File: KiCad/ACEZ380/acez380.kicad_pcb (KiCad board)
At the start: 2 copper layers, 160 x 160.8 mm, 143 parts, among them IC1 LM7805_TO220, J300 Conn_02x06_Odd_Even, J301 Conn_02x05_Odd_Even, J303 Conn_02x03_Odd_Even, J304 Conn_02x05_Odd_Even, J400 48409-0003, J402 Conn_02x06_Odd_Even, J501 Conn_02x05_Odd_Even, J502 Conn_02x03_Odd_Even, Q1 2N3904, Q100 2N3904, Q3 BC183, X1 CRYSTALHC49U-V 6.556MHz, X2 20MHz

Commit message: Remove SMD.
Standardise Z180 and add Z380.


Signed-off-by: John Bradley <flypie@rocketmail.com>
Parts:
- added J503: Conn_02x05_Odd_Even, Connector_PinHeader_2.54mm:PinHeader_2x05_P2.54mm_Vertical, F.Cu at (27.9, 54.4)
- added J604: Conn_02x03_Odd_Even, Connector_PinHeader_2.54mm:PinHeader_2x03_P2.54mm_Vertical, F.Cu at (36.2, 58.4)
- added J605: Conn_02x03_Odd_Even, Connector_PinHeader_2.54mm:PinHeader_2x03_P2.54mm_Vertical, F.Cu at (47.1, 57.8)
- added J607: Conn_02x04_Odd_Even, Connector_PinHeader_2.54mm:PinHeader_2x04_P2.54mm_Vertical, F.Cu at (81.3, 157.2)
- J300: value Conn_02x06_Odd_Even -> Conn_02x05_Odd_Even; footprint Connector_PinHeader_2.54mm:PinHeader_2x06_P2.54mm_Vertical -> Connector_PinHeader_2.54mm:PinHeader_2x05_P2.54mm_Vertical
- J303: value Conn_02x03_Odd_Even -> Conn_02x04_Odd_Even; footprint Connector_PinHeader_2.54mm:PinHeader_2x03_P2.54mm_Vertical -> Connector_PinHeader_2.54mm:PinHeader_2x04_P2.54mm_Vertical
- J304: value Conn_02x05_Odd_Even -> Conn_02x04_Odd_Even; footprint Connector_PinHeader_2.54mm:PinHeader_2x05_P2.54mm_Vertical -> Connector_PinHeader_2.54mm:PinHeader_2x04_P2.54mm_Vertical
- Z0: footprint Package_QFP:VQFP-100_14x14mm_P0.5mm -> Package_QFP:PQFP-144_28x28mm_P0.65mm
- moved Z304 224.1 mm to (173.7, 124.1)
- moved Z307 187.3 mm to (104.4, 121.5)
- moved R106 164.0 mm to (136.9, 137.5), turned to 180 degrees
- moved Z404 163.5 mm to (118.0, 98.7)
- moved R104 159.9 mm to (140.0, 137.5)
- moved R107 156.1 mm to (145.5, 137.5)
- moved R609 154.2 mm to (97.0, 59.6)
- moved R105 150.7 mm to (153.4, 137.5), turned to 180 degrees
- moved R604 150.4 mm to (97.0, 53.9)
- moved Z302 148.8 mm to (90.9, 98.4)
- moved D100 147.1 mm to (125.1, 121.5)
- moved R602 146.0 mm to (97.0, 42.7)
- moved Z407 143.8 mm to (105.7, 75.6)
- moved R603 141.4 mm to (97.0, 48.3)
- moved R601 137.3 mm to (97.0, 37.1)
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- renumbered C300 to C100, C301 to C101
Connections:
- D100 pad 1: ~INT2 -> ~INT3
- J301 pad 4: PB6 -> (no net)
- J301 pad 6: PB5 -> (no net)
- J301 pad 7: PB3 -> (no net)
- J301 pad 8: PB4 -> (no net)
- J303 pad 1: TxDA -> TxA0
- J303 pad 2: RxDA -> RxA0
- J303 pad 3: ~TRxCA -> ~RTS0
- J303 pad 4: ~RTxCA -> ~CTS0
- J303 pad 5: +5V -> ~DCD0
- J303 pad 6: GND -> CKA0
- J304 pad 1: TxDB -> TxA1
- J304 pad 2: RxDB -> RxA1
- J304 pad 3: ~TRxCB -> ~RTS1
- J304 pad 4: ~DCDB -> ~CTS1
- J304 pad 5: ~RTxCB -> ~DCD1
- J304 pad 6: ~CTSB -> CKA1
- J304 pad 7: ~SYNCB -> +5V
- J304 pad 8: ~RTSB -> GND
- J501 pad 1: PC0 -> (no net)
- J501 pad 2: (no net) -> PC7
- J501 pad 3: PC1 -> (no net)
- J501 pad 7: PC3 -> (no net)
- Z0 pad 1: (no net) -> A19
- Z0 pad 10: A8 -> A11
- Z0 pad 100: ~INT2 -> TxC1
- Z0 pad 11: A9 -> A10
- Z0 pad 12: A10 -> A9
- Z0 pad 13: A11 -> A8
- Z0 pad 14: A12 -> GND
- Z0 pad 15: +5V -> A7
- Z0 pad 16: A13 -> A6
- Z0 pad 17: A14 -> A5
- Z0 pad 18: A15 -> A4
- Z0 pad 19: A16 -> A3
- Z0 pad 2: A0 -> A18
- Z0 pad 20: A17 -> A2
- Z0 pad 21: A18 -> A1
- Z0 pad 22: GND -> A0
- Z0 pad 23: A19 -> +5V
- Z0 pad 24: DA0 -> (no net)
- Z0 pad 25: DA1 -> (no net)
- Z0 pad 26: DA2 -> (no net)
- Z0 pad 27: DA3 -> (no net)
- Z0 pad 28: DA4 -> (no net)
- Z0 pad 29: DA5 -> (no net)
- Z0 pad 3: A1 -> A17
- Z0 pad 30: DA6 -> (no net)
- Z0 pad 31: DA7 -> (no net)
- Z0 pad 32: PB0 -> GND
- Z0 pad 33: PB1 -> DA7
- Z0 pad 34: PB2 -> DA6
- Z0 pad 35: PB3 -> DA5
- Z0 pad 36: PB4 -> DA4
- Z0 pad 37: PB5 -> DA3
- Z0 pad 38: PB6 -> DA2
- Z0 pad 39: RxS\~CTS -> DA1
- Z0 pad 4: A2 -> A16
- Z0 pad 40: (no net) -> DA0
- Z0 pad 41: GND -> +5V
- Z0 pad 43: TxS -> ~MREQ
- Z0 pad 44: CKS -> PC7
- Z0 pad 45: (no net) -> PC6
- Z0 pad 46: +5V -> (no net)
- Z0 pad 47: ~RTSB -> PC5
- Z0 pad 48: (no net) -> PC4
- Z0 pad 49: (no net) -> CKA1
- Z0 pad 5: A3 -> +5V
- Z0 pad 51: (no net) -> TxA0
- Z0 pad 52: PA0 -> RxA0
- Z0 pad 53: PA1 -> CKA0
- Z0 pad 54: PA2 -> TxA1
- Z0 pad 55: PA3 -> RxA1
- Z0 pad 56: PA4 -> PB2
- Z0 pad 57: PA5 -> PB1
- Z0 pad 58: PA6 -> PB0
- Z0 pad 59: PA7 -> +5V
- Z0 pad 6: A4 -> A15
- Z0 pad 60: PC5 -> ~CTS1
- Z0 pad 61: PC3 -> ~CTS0
- Z0 pad 62: PC2 -> TxS
- Z0 pad 63: PC1 -> RxS\~CTS
- Z0 pad 64: PC0 -> CKS
- Z0 pad 65: PC4 -> CKA1
- Z0 pad 66: ~RTxCA -> ~DCD1
- Z0 pad 67: GND -> RxD1
- Z0 pad 68: (no net) -> GND
- Z0 pad 69: (no net) -> PD7
- Z0 pad 7: A5 -> A14
- Z0 pad 70: +5V -> PD6
- Z0 pad 71: RxDA -> PD5
- Z0 pad 72: ~TRxCA -> PD4
- Z0 pad 73: TxDA -> PD3
- Z0 pad 74: ~DCDB -> PD2
- Z0 pad 75: ~CTSB -> PD1
- Z0 pad 76: TxDB -> PD0
- Z0 pad 77: ~TRxCB -> +5V
- Z0 pad 78: RxDB -> PA7
- Z0 pad 79: ~RTxCB -> PA6
- Z0 pad 8: A6 -> A13
- Z0 pad 80: ~SYNCB -> PA5
- Z0 pad 81: /~HALT -> PA4
- Z0 pad 82: ~RFSH -> PA3
- Z0 pad 83: ~IOREQ -> PA2
- Z0 pad 84: ~MREQ -> PA1
- Z0 pad 85: (no net) -> PA0
- Z0 pad 86: ~M1 -> +5V
- Z0 pad 87: ~WR -> TxA1
- Z0 pad 88: ~RD -> (no net)
- Z0 pad 89: ~CPUCLK -> ~DCD0
- Z0 pad 9: A7 -> A12
- Z0 pad 90: GND -> RxA0
- Z0 pad 91: Net-(C101-Pad2) -> TxA0
- Z0 pad 92: Net-(C100-Pad2) -> CKA0
- Z0 pad 93: /~WAIT -> ~RTS0
- Z0 pad 94: /~BUSAK -> ~RTS1
- Z0 pad 95: /~BUSRQ -> +5V
- Z0 pad 96: ~RESET -> TxC0
- Z0 pad 97: ~NMI -> RxC0
- Z0 pad 98: ~INT0 -> TxD0
- Z0 pad 99: PC6 -> RxD0
- Z24 pad 3: ~WR -> ~IOWR
- Z24 pad 6: ~RD -> ~IORD
- Z3-4 pad 17: ~WR -> ~MWR
- Z3-4 pad 41: ~RD -> ~MRD
- Z408 pad 13: RxDB -> RxD2
- Z408 pad 14: TxDB -> TxD2
- Z80CPUOUT1 pad 18: ~RFSH -> (no net)
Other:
- board text added: "Jupiter Ace Z382"
- board text removed: "Jupiter Ace Z180"

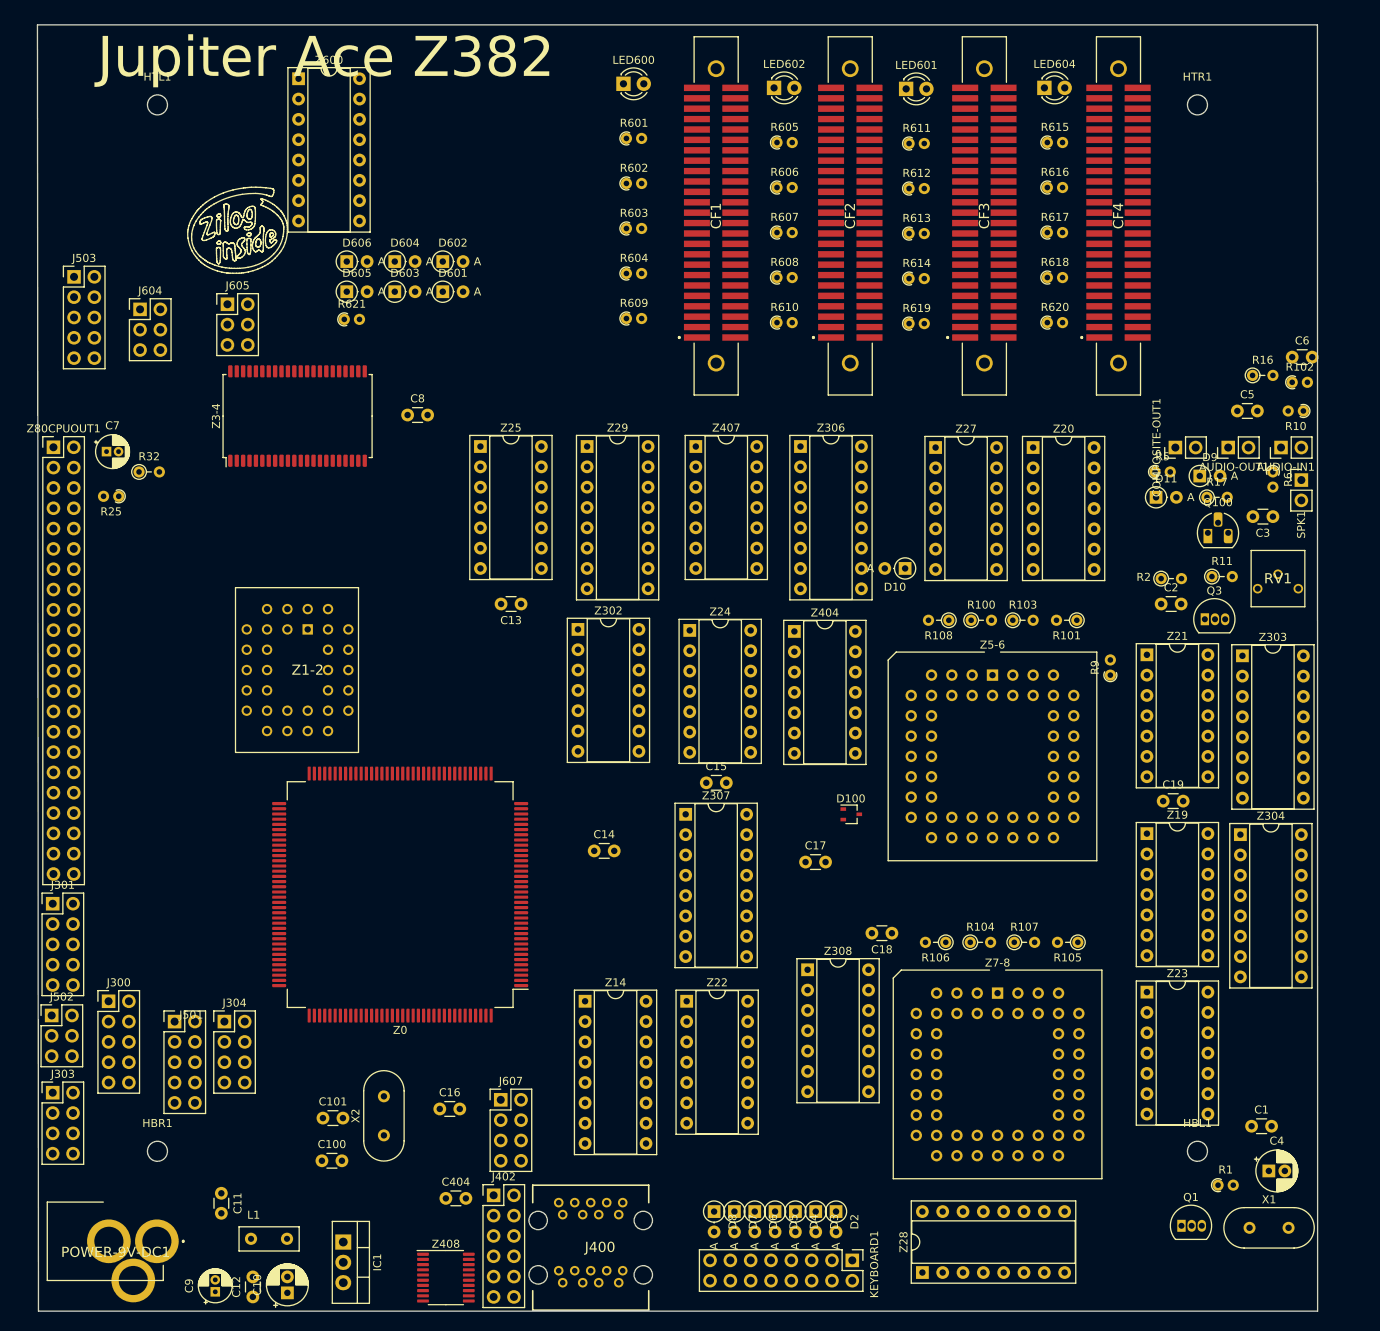
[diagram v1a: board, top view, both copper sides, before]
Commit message: Update ACE3NOKB to reflect errors in Mem Decode. ACE5NOKB test SMT ideas. Added 180 & 380.
Signed-off-by: John Bradley <flypie@rocketmail.com>
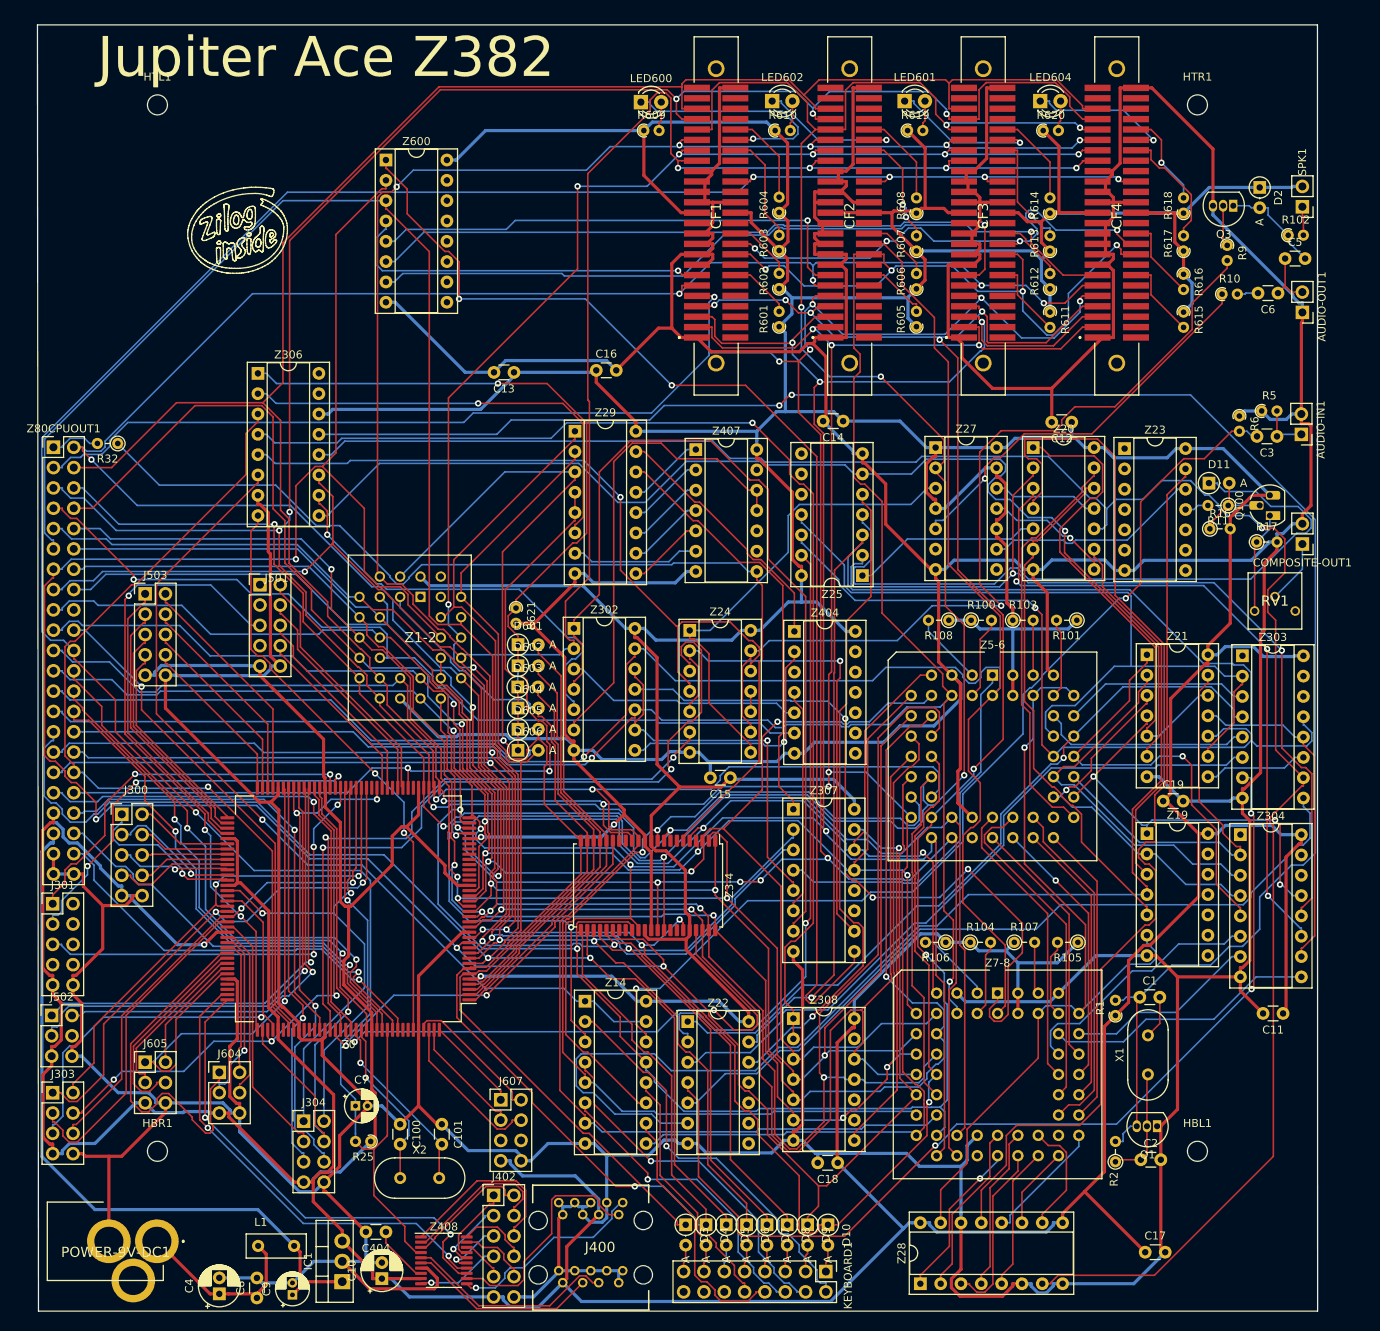
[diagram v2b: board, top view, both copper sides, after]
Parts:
- removed D100: BAT54W, Package_TO_SOT_SMD:SOT-323_SC-70
- moved C12 149.8 mm to (152.7, 72.5), turned to 180 degrees
- moved D2 138.5 mm to (176.1, 43.2)
- moved C11 134.6 mm to (179.1, 146.4), turned to 180 degrees
- moved C4 132.1 mm to (46.1, 181.5), turned to 90 degrees
- moved C8 112.0 mm to (50.8, 182.0), turned to 90 degrees
- moved D9 105.7 mm to (119.6, 172.8), turned to 270 degrees
- moved J604 95.9 mm to (46.1, 153.8)
- moved J605 95.3 mm to (36.8, 152.5)
- moved C16 94.4 mm to (93.2, 66.0)
- moved C7 87.5 mm to (63.1, 158.0)
- moved R25 86.6 mm to (65.0, 162.4)
- moved D10 82.6 mm to (122.2, 172.8), turned to 270 degrees
- moved Z3-4 73.2 mm to (99.7, 130.4), turned to 270 degrees
- moved R2 73.1 mm to (158.1, 165.0), turned to 90 degrees
- moved C2 69.5 mm to (161.3, 164.7)
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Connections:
- Z306 pad 8: Net-(D100-Pad3) -> ~INT3
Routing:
- net GND: track 0.00 -> 1378.5 mm, vias 0 -> 2
- net +5V: track 0.00 -> 1362.7 mm, vias 0 -> 2
- net DA0: track 0.00 -> 406.7 mm, vias 0 -> 9
- net DA2: track 0.00 -> 399.9 mm, vias 0 -> 2
- net DA1: track 0.00 -> 389.8 mm, vias 0 -> 8
- net DA7: track 0.00 -> 376.8 mm, vias 0 -> 8
- net DA6: track 0.00 -> 367.1 mm, vias 0 -> 11
- net A12: track 0.00 -> 353.6 mm, vias 0 -> 8
- net DA4: track 0.00 -> 351.2 mm, vias 0 -> 7
- net DA5: track 0.00 -> 348.1 mm, vias 0 -> 9
- net A9: track 0.00 -> 338.5 mm, vias 0 -> 4
- net A10: track 0.00 -> 336.5 mm, vias 0 -> 7
- net A11: track 0.00 -> 333.1 mm, vias 0 -> 10
- net DA3: track 0.00 -> 326.4 mm, vias 0 -> 7
- net A8: track 0.00 -> 317.3 mm, vias 0 -> 5
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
